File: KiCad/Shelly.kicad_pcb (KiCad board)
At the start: 2 copper layers, 16 x 30 mm, 15 parts, among them J1 Shelly 1, J2 Shelly 2, J3 Shelly i3, J4 USB-C, M1 D24V5F3-NoSHDN, U1 FT231XQ, U2 TLP3546

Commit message: Moved resistor
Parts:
- moved R3 0.50 mm to (173.3, 71.9)
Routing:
- net +3V3: track 29.8 -> 31.1 mm
- net Net-(D1-Pad2): track 15.5 -> 14.7 mm
- net Net-(D1-Pad1): track 21.2 -> 21.8 mm

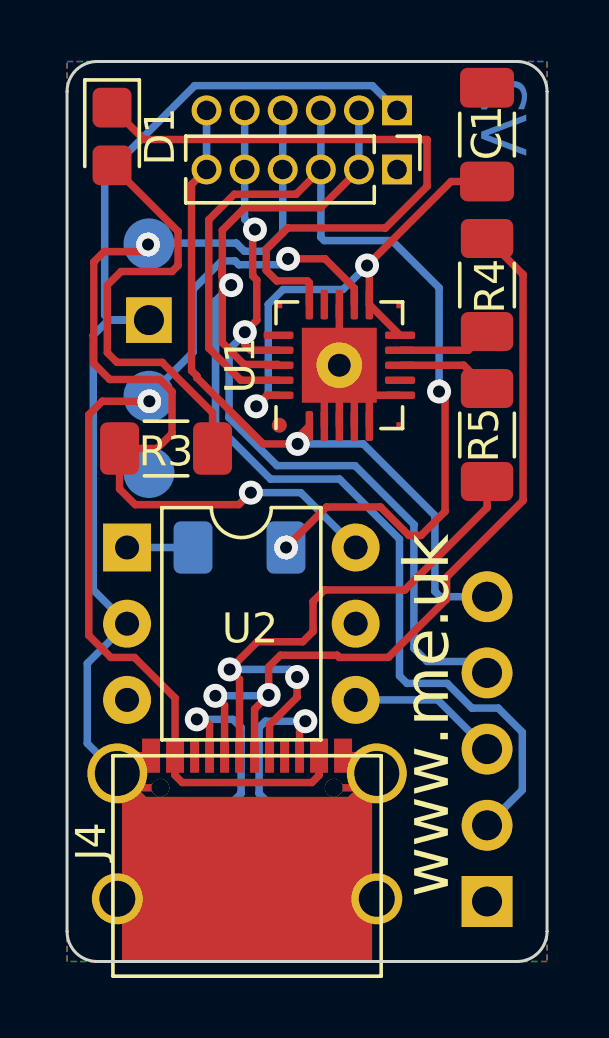
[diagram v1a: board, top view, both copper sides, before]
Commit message: Change to smaller compnent
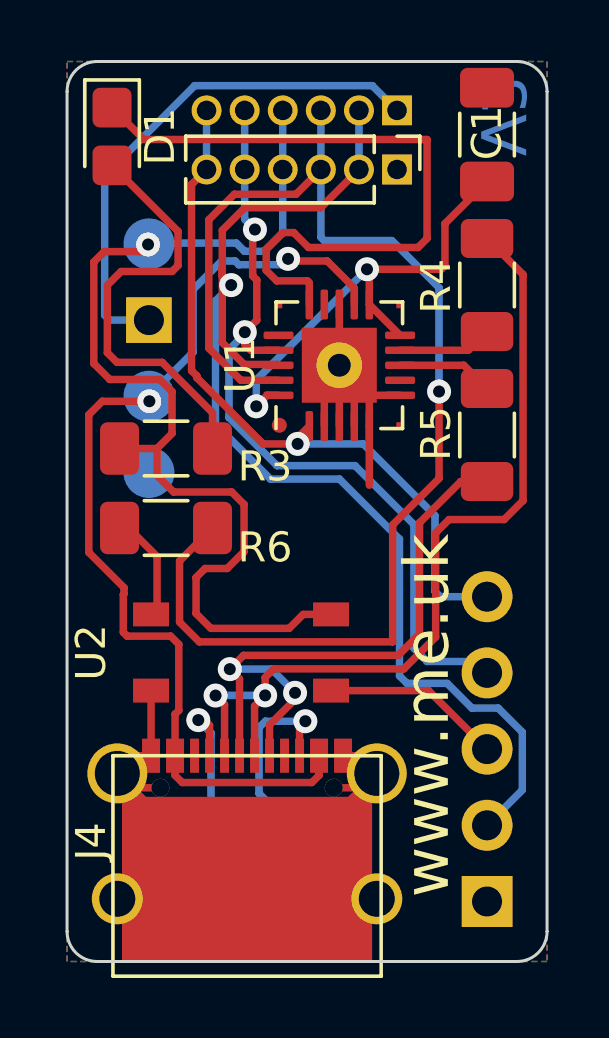
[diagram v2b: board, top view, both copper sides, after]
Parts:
- R6: moved to F.Cu
- U2: value TLP3546 -> G3VM-61VY3(TR); footprint Package_DIP:DIP-6_W7.62mm -> RevK:Special-SOP-4-3.7x4.55
- moved U2 5.17 mm to (175.8, 78.7), turned to 270 degrees
- moved R6 2.53 mm to (173.3, 74.5)
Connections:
- U2 pad 3: Net-(U2-Pad3) -> Net-(J1-Pad3)
- U2 pad 4: Net-(J1-Pad3) -> +3V3
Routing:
- net GND: track 69.8 -> 55.8 mm
- net RST: track 34.5 -> 44.6 mm, vias 2 -> 1
- net +3V3: track 31.1 -> 34.5 mm, vias 2 -> 1
- net Net-(J4-PadA5): track 6.72 -> 5.09 mm
- net Net-(R6-Pad1): track 2.20 -> 3.66 mm
- net Net-(D1-Pad1): track 21.8 -> 23.2 mm
- net Net-(J4-PadA7): track 27.6 -> 28.8 mm
- net Net-(J1-Pad3): track 5.06 -> 6.01 mm
- net Net-(J4-PadA6): track 20.6 -> 21.3 mm
- net Net-(C1-Pad1): track 16.2 -> 15.7 mm
- net VBUS: track 32.6 -> 33.1 mm
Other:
- board text added: "V3"
- board text removed: "V2"

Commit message: Reworked to be smaller (15x30)
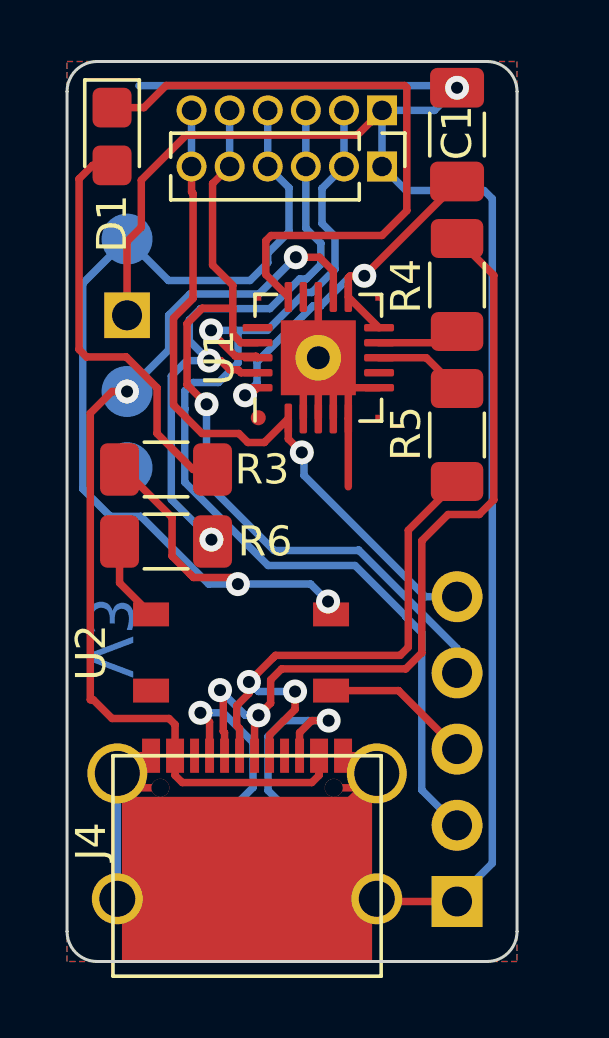
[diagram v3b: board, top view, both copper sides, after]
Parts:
- moved C1 1.00 mm to (183.0, 61.4)
- moved J1 1.00 mm to (183.0, 87.0)
- moved R4 1.00 mm to (183.0, 66.5)
- moved R5 1.00 mm to (183.0, 71.5)
- moved M1 0.75 mm to (170.7, 68.7)
- moved U1 0.74 mm to (178.4, 68.9)
- moved R3 0.70 mm to (173.3, 72.6)
- moved J3 0.51 mm to (180.5, 62.5)
- moved J2 0.50 mm to (180.5, 60.6)
- moved R6 0.45 mm to (173.3, 75.0)
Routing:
- net GND: track 55.8 -> 99.2 mm, vias 0 -> 1
- net RST: track 44.6 -> 21.4 mm, vias 1 -> 2
- net GPIO0: track 39.6 -> 35.9 mm
- net Net-(J4-PadA6): track 21.3 -> 18.8 mm
- net +3V3: track 34.5 -> 36.6 mm, vias 1 -> 2
- net Net-(C1-Pad1): track 15.7 -> 13.6 mm
- net Net-(J4-PadA5): track 5.09 -> 7.12 mm
- net Net-(D1-Pad1): track 23.2 -> 21.6 mm
- net VBUS: track 33.1 -> 32.0 mm
- net Net-(J1-Pad3): track 6.01 -> 5.01 mm
- net Net-(J4-PadA7): track 28.8 -> 28.0 mm
- net Net-(R6-Pad1): track 3.66 -> 2.86 mm
- net RXD: track 27.0 -> 27.7 mm, vias 2 -> 1
- net Net-(D1-Pad2): track 14.7 -> 14.0 mm
- net Net-(J4-PadB5): track 6.75 -> 7.42 mm
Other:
- board size 16 x 30 mm -> 15 x 30 mm
- board text removed: "www.me.uk"
